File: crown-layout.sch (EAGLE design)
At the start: 15 parts

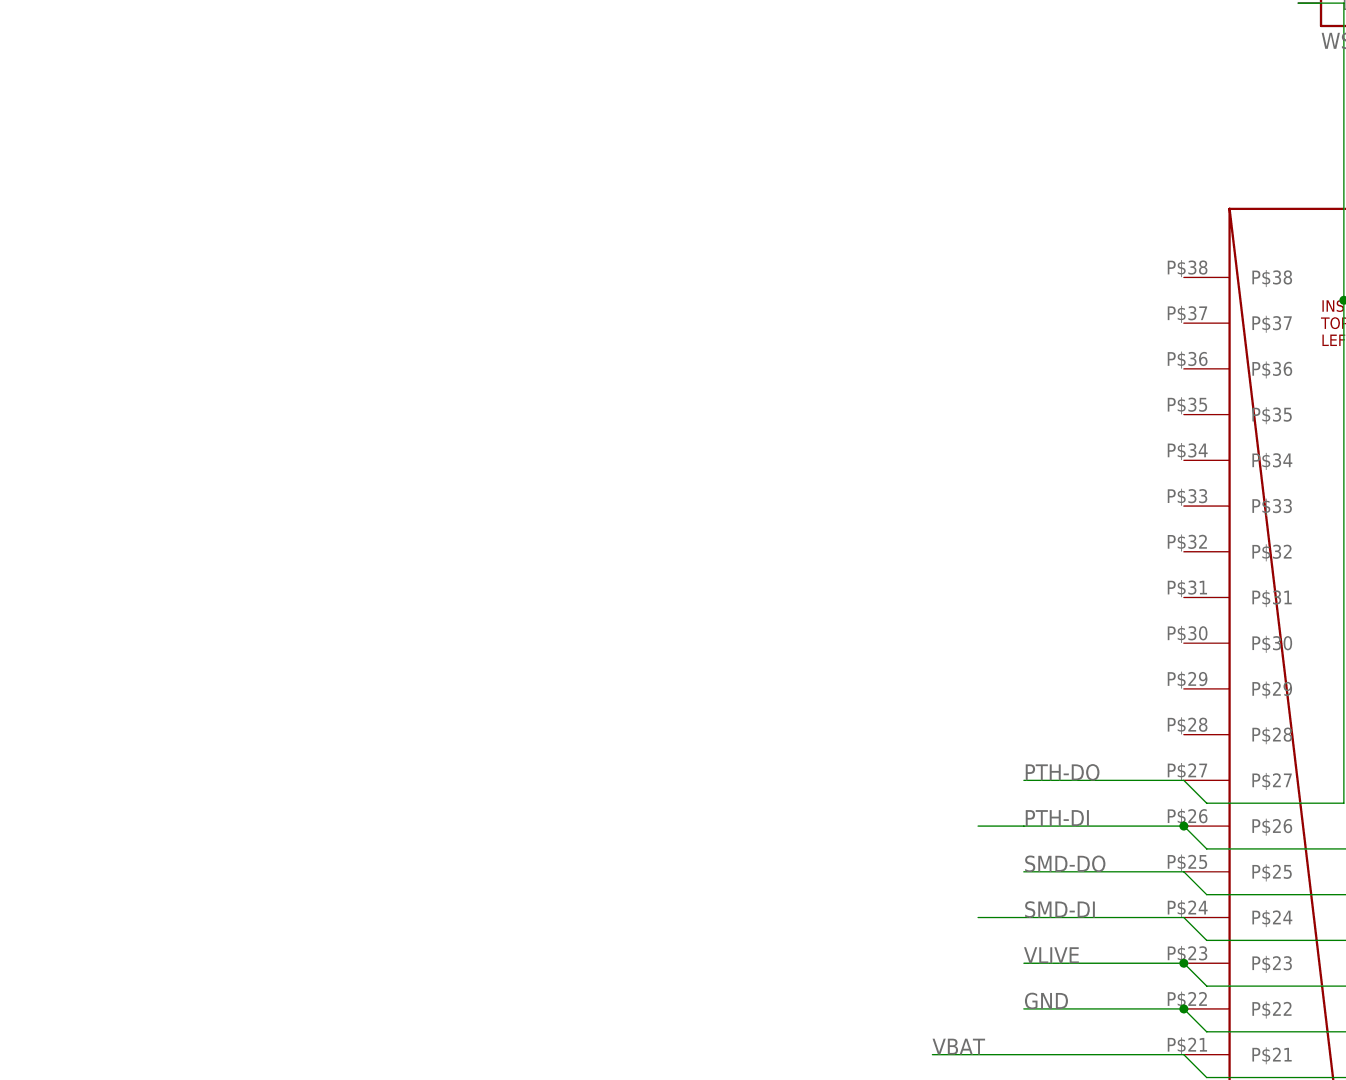
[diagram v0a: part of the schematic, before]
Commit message: Made B board, looks a bit funky on the routing.
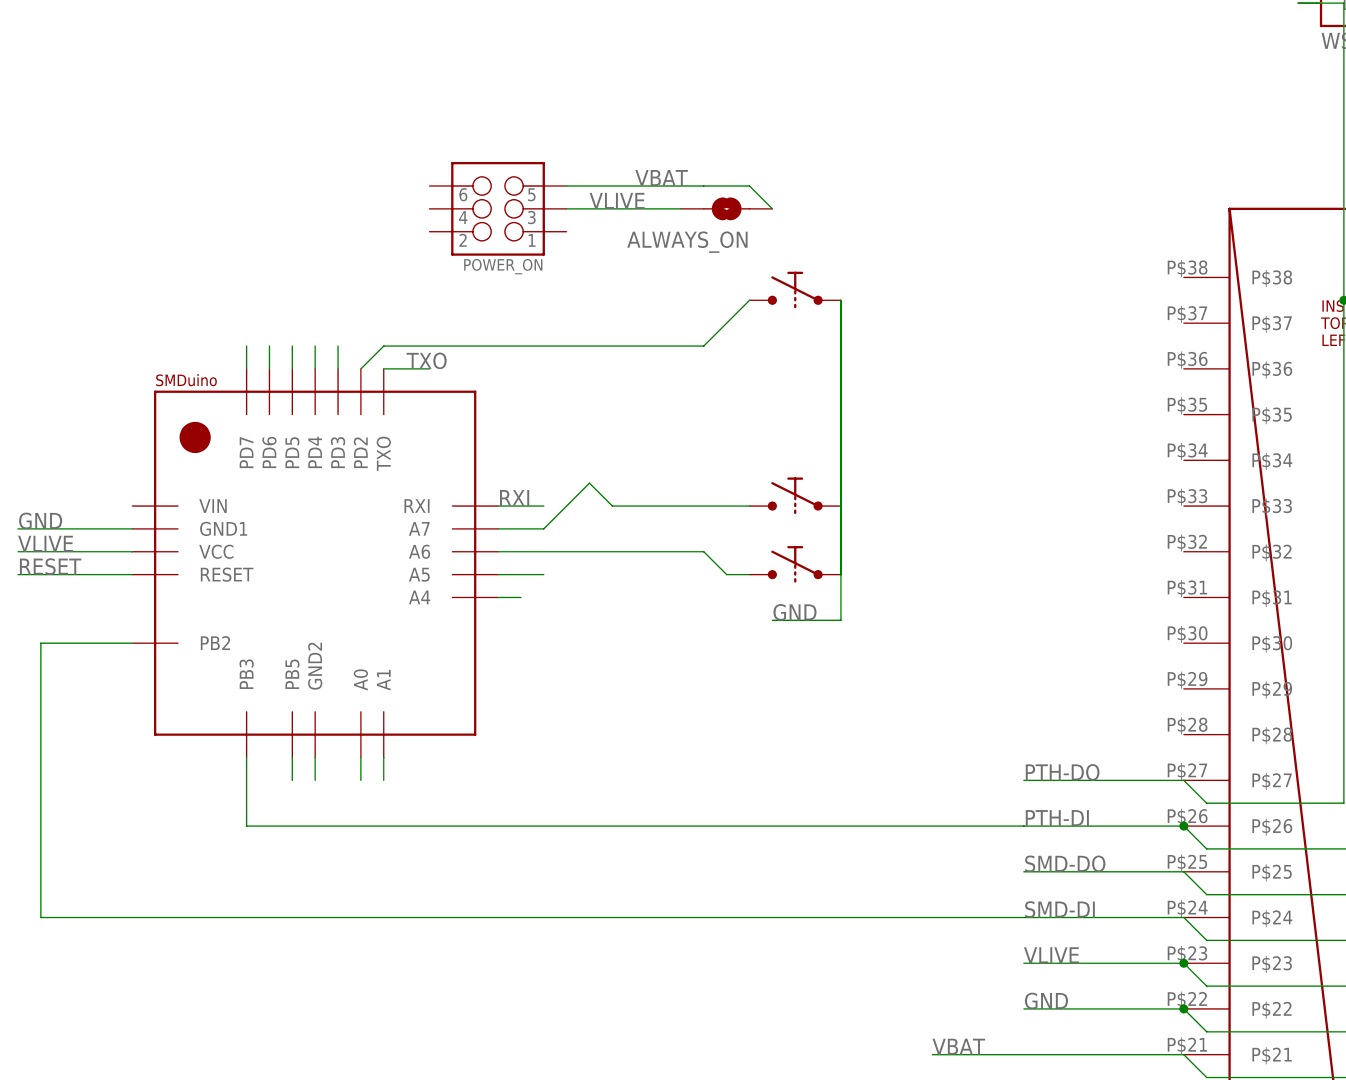
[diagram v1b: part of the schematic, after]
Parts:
- added A6, A7, D2: BUTTONSMD_BUTTON, tekdemo:BUTTONSMD_BUTTON
- added ALWAYS_ON: SOLDERJUMPERNC2, SparkFun-Passives:SOLDERJUMPERNC2
- added POWER_ON: (no value), SparkFun-Connectors:M03X2FEMALE_SMD
- added U$1: SMDUINODIS-CONNECTED-PINS, pcb_crown:SMDUINODIS-CONNECTED-PINS
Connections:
- new net N$12: U$1.PB5
- new net N$13: U$1.GND2
- new net N$14: U$1.A0
- new net N$15: U$1.A1
- new net N$16: U$1.PD7
- new net N$17: U$1.PD6
- new net N$18: U$1.PD5
- new net N$19: U$1.PD4
- new net N$2: A7.P$1, U$1.A7
- new net N$20: U$1.PD3
- new net N$6: A6.P$1, U$1.A6
- new net N$7: U$1.A5
- new net N$8: U$1.A4
- new net N$9: D2.P$1, U$1.PD2
- new net RESET: U$1.RESET
- new net RXI: U$1.RXI
- new net TXO: U$1.TXO
- net GND: now also A6.P$2, A7.P$2, D2.P$2, U$1.GND1
- net PTH-DI: now also U$1.PB3
- net SMD-DI: now also U$1.PB2
- net VBAT: now also ALWAYS_ON.1, POWER_ON.5
- net VLIVE: now also ALWAYS_ON.2, POWER_ON.3, U$1.VCC
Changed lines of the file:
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@@
 <part name="PTH-END-NODE" library="SparkFun-Passives" deviceset="RESISTOR" device="0805-RES" value="300-500 OHM"/>
 <part name="SMD-END-NODE" library="SparkFun-Passives" deviceset="RESISTOR" device="0805-RES" value="300-500 OHM"/>
+<part name="POWER_ON" library="SparkFun-Connectors" deviceset="M03X2" device="FEMALE_SMD"/>
+<part name="A7" library="tekdemo" deviceset="BUTTON" device="SMD_BUTTON"/>
+<part name="A6" library="tekdemo" deviceset="BUTTON" device="SMD_BUTTON"/>
+<part name="D2" library="tekdemo" deviceset="BUTTON" device="SMD_BUTTON"/>
+<part name="U$1" library="pcb_crown" deviceset="SMDUINO" device="DIS-CONNECTED-PINS"/>
+<part name="ALWAYS_ON" library="SparkFun-Passives" deviceset="SOLDERJUMPER" device="NC2" value=""/>
 </parts>
 <sheets>
@@
 <instance part="PTH-END-NODE" gate="G$1" x="162.56" y="35.56" rot="R90"/>
 <instance part="SMD-END-NODE" gate="G$1" x="144.78" y="20.32"/>
+<instance part="POWER_ON" gate="G$1" x="-27.94" y="99.06" rot="R180"/>
+<instance part="A7" gate="G$1" x="5.08" y="66.04"/>
+<instance part="A6" gate="G$1" x="5.08" y="58.42"/>
+<instance part="D2" gate="G$1" x="5.08" y="88.9"/>
+<instance part="U$1" gate="G$1" x="-66.04" y="40.64"/>
+<instance part="ALWAYS_ON" gate="1" x="-2.54" y="99.06" rot="R180"/>
 </instances>
 <busses>
@@
 <label x="81.28" y="142.24" size="1.778" layer="95"/>
 </segment>
+<segment>
+<wire x1="-68.58" y1="63.5" x2="-81.28" y2="63.5" width="0.2032" layer="91"/>
+<label x="-81.28" y="63.5" size="1.778" layer="95"/>
+<pinref part="U$1" gate="G$1" pin="GND1"/>
+</segment>
+<segment>
+<pinref part="A7" gate="G$1" pin="P$2"/>
+<pinref part="A6" gate="G$1" pin="P$2"/>
+<wire x1="10.16" y1="66.04" x2="10.16" y2="58.42" width="0.2032" layer="91"/>
+<pinref part="D2" gate="G$1" pin="P$2"/>
+<wire x1="10.16" y1="58.42" x2="10.16" y2="88.9" width="0.2032" layer="91"/>
+<wire x1="10.16" y1="88.9" x2="10.16" y2="53.34" width="0.2032" layer="91"/>
+<wire x1="10.16" y1="53.34" x2="2.54" y2="53.34" width="0.2032" layer="91"/>
+<label x="2.54" y="53.34" size="1.778" layer="95"/>
+</segment>
 </net>
 <net name="VLIVE" class="0">
@@
 </segment>
 <segment>
+<pinref part="U$1" gate="G$1" pin="VCC"/>
+<wire x1="-68.58" y1="60.96" x2="-81.28" y2="60.96" width="0.2032" layer="91"/>
+<label x="-81.28" y="60.96" size="1.778" layer="95"/>
+<wire x1="-7.62" y1="99.06" x2="-20.32" y2="99.06" width="0.2032" layer="91"/>
+<label x="-17.78" y="99.06" size="1.778" layer="95"/>
+<pinref part="POWER_ON" gate="G$1" pin="3"/>
+<pinref part="ALWAYS_ON" gate="1" pin="2"/>
+</segment>
+<segment>
 <pinref part="SMD1" gate="G$1" pin="VDD"/>
 <wire x1="226.06" y1="71.12" x2="223.52" y2="68.58" width="0.2032" layer="91"/>
@@
 <pinref part="U$2" gate="G$1" pin="P$7"/>
 <pinref part="PTH-END-NODE" gate="G$1" pin="1"/>
-<wire x1="30.48" y1="30.48" x2="25.4" y2="30.48" width="0.2032" layer="91"/>
+<wire x1="30.48" y1="30.48" x2="-55.88" y2="30.48" width="0.2032" layer="91"/>
+<pinref part="U$1" gate="G$1" pin="PB3"/>
+<wire x1="-55.88" y1="30.48" x2="-55.88" y2="38.1" width="0.2032" layer="91"/>
 </segment>
 </net>
@@
 <label x="144.78" y="5.08" size="1.778" layer="95"/>
 </segment>
+<segment>
+<wire x1="-5.08" y1="101.6" x2="-20.32" y2="101.6" width="0.2032" layer="91"/>
+<label x="-12.7" y="101.6" size="1.778" layer="95"/>
+<pinref part="POWER_ON" gate="G$1" pin="5"/>
+<pinref part="ALWAYS_ON" gate="1" pin="1"/>
+<wire x1="2.54" y1="99.06" x2="0" y2="101.6" width="0.1524" layer="91"/>
+<wire x1="0" y1="101.6" x2="-5.08" y2="101.6" width="0.1524" layer="91"/>
+</segment>
 </net>
 <net name="N$5" class="0">
@@
 <pinref part="SMD-END-NODE" gate="G$1" pin="1"/>
 <junction x="139.7" y="20.32"/>
-<wire x1="48.26" y1="20.32" x2="25.4" y2="20.32" width="0.2032" layer="91"/>
+<wire x1="48.26" y1="20.32" x2="-78.74" y2="20.32" width="0.2032" layer="91"/>
+<pinref part="U$1" gate="G$1" pin="PB2"/>
+<wire x1="-68.58" y1="50.8" x2="-78.74" y2="50.8" width="0.2032" layer="91"/>
+<wire x1="-78.74" y1="20.32" x2="-78.74" y2="50.8" width="0.2032" layer="91"/>
 </segment>
 </net>
@@
 </segment>
 </net>
+<net name="RESET" class="0">
+<segment>
+<wire x1="-68.58" y1="58.42" x2="-81.28" y2="58.42" width="0.2032" layer="91"/>
+<label x="-81.28" y="58.42" size="1.778" layer="95"/>
+<pinref part="U$1" gate="G$1" pin="RESET"/>
+</segment>
+</net>
+<net name="RXI" class="0">
+<segment>
+<wire x1="-27.94" y1="66.04" x2="-22.86" y2="66.04" width="0.2032" layer="91"/>
+<label x="-27.94" y="66.04" size="1.778" layer="95"/>
+<pinref part="U$1" gate="G$1" pin="RXI"/>
+</segment>
+</net>
+<net name="TXO" class="0">
+<segment>
+<wire x1="-40.64" y1="81.28" x2="-35.56" y2="81.28" width="0.2032" layer="91"/>
+<label x="-38.1" y="81.28" size="1.778" layer="95"/>
+<pinref part="U$1" gate="G$1" pin="TXO"/>
+</segment>
+</net>
+<net name="N$2" class="0">
+<segment>
+<pinref part="U$1" gate="G$1" pin="A7"/>
+<wire x1="-27.94" y1="63.5" x2="-22.86" y2="63.5" width="0.2032" layer="91"/>
+<wire x1="-22.86" y1="63.5" x2="-17.78" y2="68.58" width="0.2032" layer="91"/>
+<wire x1="-17.78" y1="68.58" x2="-15.24" y2="66.04" width="0.2032" layer="91"/>
+<pinref part="A7" gate="G$1" pin="P$1"/>
+<wire x1="-15.24" y1="66.04" x2="0" y2="66.04" width="0.2032" layer="91"/>
+</segment>
+</net>
+<net name="N$6" class="0">
+<segment>
+<pinref part="U$1" gate="G$1" pin="A6"/>
+<wire x1="-27.94" y1="60.96" x2="-5.08" y2="60.96" width="0.2032" layer="91"/>
+<pinref part="A6" gate="G$1" pin="P$1"/>
+<wire x1="-5.08" y1="60.96" x2="-2.54" y2="58.42" width="0.2032" layer="91"/>
+<wire x1="-2.54" y1="58.42" x2="0" y2="58.42" width="0.2032" layer="91"/>
+</segment>
+</net>
+<net name="N$7" class="0">
+<segment>
+<pinref part="U$1" gate="G$1" pin="A5"/>
+<wire x1="-27.94" y1="58.42" x2="-22.86" y2="58.42" width="0.2032" layer="91"/>
+</segment>
+</net>
+<net name="N$8" class="0">
+<segment>
+<pinref part="U$1" gate="G$1" pin="A4"/>
+<wire x1="-27.94" y1="55.88" x2="-25.4" y2="55.88" width="0.2032" layer="91"/>
+</segment>
+</net>
+<net name="N$9" class="0">
+<segment>
+<pinref part="U$1" gate="G$1" pin="PD2"/>
+<wire x1="-43.18" y1="81.28" x2="-40.64" y2="83.82" width="0.2032" layer="91"/>
+<pinref part="D2" gate="G$1" pin="P$1"/>
+<wire x1="0" y1="88.9" x2="-5.08" y2="83.82" width="0.2032" layer="91"/>
+<wire x1="-5.08" y1="83.82" x2="-40.64" y2="83.82" width="0.2032" layer="91"/>
+</segment>
+</net>
 <net name="N$10" class="0">
 <segment>
@@
 </segment>
 </net>
+<net name="N$12" class="0">
+<segment>
+<pinref part="U$1" gate="G$1" pin="PB5"/>
+<wire x1="-50.8" y1="38.1" x2="-50.8" y2="35.56" width="0.2032" layer="91"/>
+</segment>
+</net>
+<net name="N$13" class="0">
+<segment>
+<pinref part="U$1" gate="G$1" pin="GND2"/>
+<wire x1="-48.26" y1="38.1" x2="-48.26" y2="35.56" width="0.2032" layer="91"/>
+</segment>
+</net>
+<net name="N$14" class="0">
+<segment>
+<pinref part="U$1" gate="G$1" pin="A0"/>
+<wire x1="-43.18" y1="38.1" x2="-43.18" y2="35.56" width="0.2032" layer="91"/>
+</segment>
+</net>
+<net name="N$15" class="0">
+<segment>
+<pinref part="U$1" gate="G$1" pin="A1"/>
+<wire x1="-40.64" y1="38.1" x2="-40.64" y2="35.56" width="0.2032" layer="91"/>
+</segment>
+</net>
+<net name="N$16" class="0">
+<segment>
+<pinref part="U$1" gate="G$1" pin="PD7"/>
+<wire x1="-55.88" y1="81.28" x2="-55.88" y2="83.82" width="0.2032" layer="91"/>
+</segment>
+</net>
+<net name="N$17" class="0">
+<segment>
+<pinref part="U$1" gate="G$1" pin="PD6"/>
+<wire x1="-53.34" y1="81.28" x2="-53.34" y2="83.82" width="0.2032" layer="91"/>
+</segment>
+</net>
+<net name="N$18" class="0">
+<segment>
+<pinref part="U$1" gate="G$1" pin="PD5"/>
+<wire x1="-50.8" y1="81.28" x2="-50.8" y2="83.82" width="0.2032" layer="91"/>
+</segment>
+</net>
+<net name="N$19" class="0">
+<segment>
+<pinref part="U$1" gate="G$1" pin="PD4"/>
+<wire x1="-48.26" y1="81.28" x2="-48.26" y2="83.82" width="0.2032" layer="91"/>
+</segment>
+</net>
+<net name="N$20" class="0">
+<segment>
+<pinref part="U$1" gate="G$1" pin="PD3"/>
+<wire x1="-45.72" y1="81.28" x2="-45.72" y2="83.82" width="0.2032" layer="91"/>
+</segment>
+</net>
